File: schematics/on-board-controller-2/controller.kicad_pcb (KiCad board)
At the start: 2 copper layers, 90 x 60 mm, 75 parts, among them J1 5-1814832-1, J2 programmer, J3 xt60, M1 Motor_DC, M2 Motor_DC, M3 Stepper_Motor_bipolar, Q1 NMOS, U1 L293D, U2 STM32L476RGTx, U3 L293D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

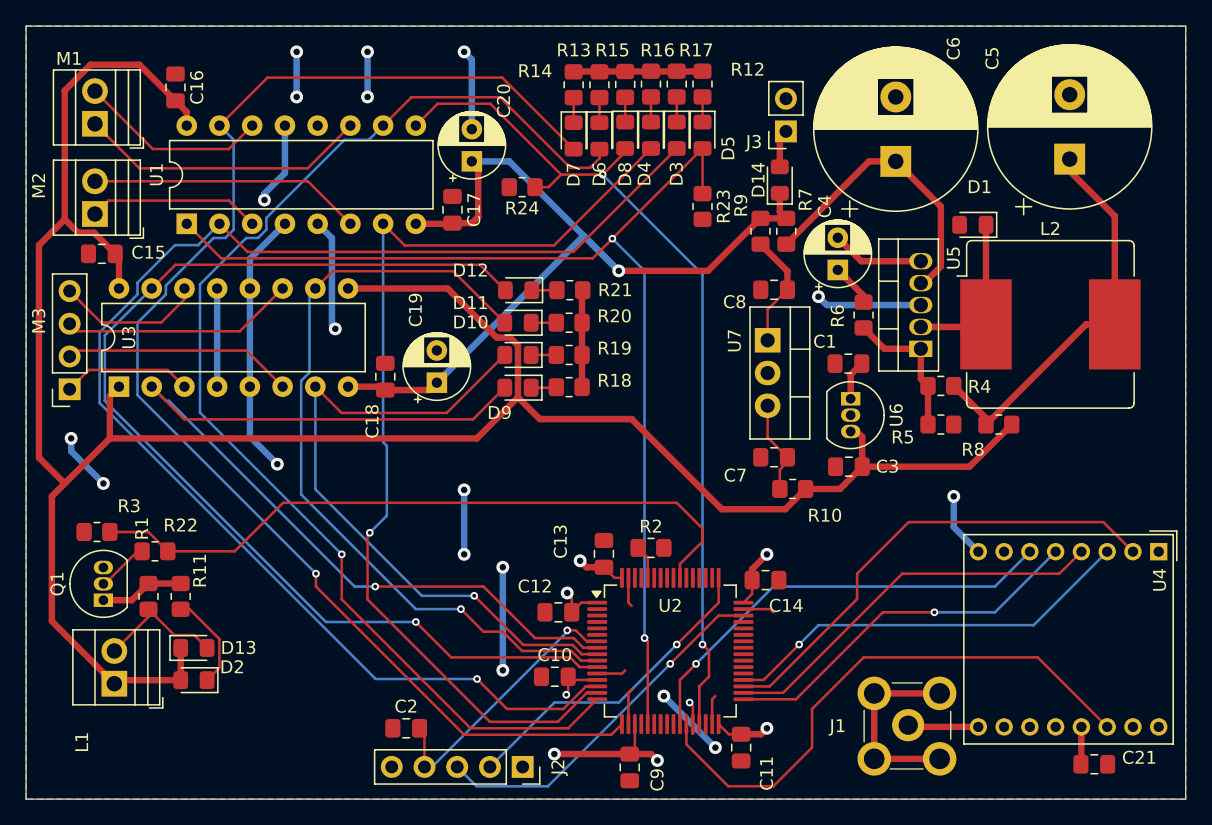
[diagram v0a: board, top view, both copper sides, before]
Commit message: produced version with 2 0V floods
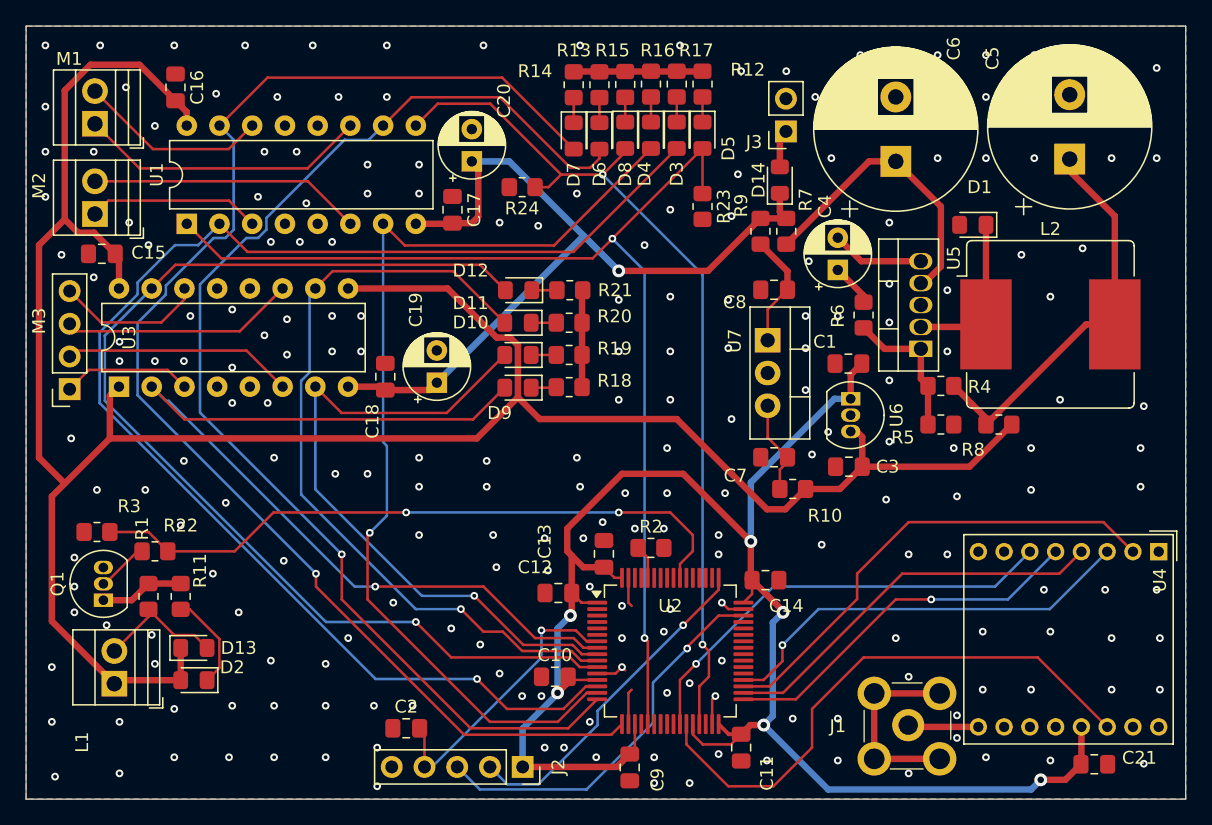
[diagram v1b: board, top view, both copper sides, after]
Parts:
- moved C12 1.50 mm to (103.8, 104.5)
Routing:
- net +3V3: track 40.3 -> 136.9 mm, vias 8 -> 6
- net GND: track 140.5 -> 46.9 mm, vias 18 -> 222
- net /mcu/SWDIO: track 28.3 -> 30.4 mm
- net ELECTROMAGNET: track 53.6 -> 51.6 mm, vias 0 -> 2
- net /mcu/SWCLK: track 25.0 -> 26.1 mm
- net /mcu/RESET: track 21.4 -> 22.5 mm
- net MOSI: track 32.4 -> 33.1 mm
- added copper zone on B.Cu, net GND
- removed copper zone on B.Cu, net +3V3

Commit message: added a keepout zone
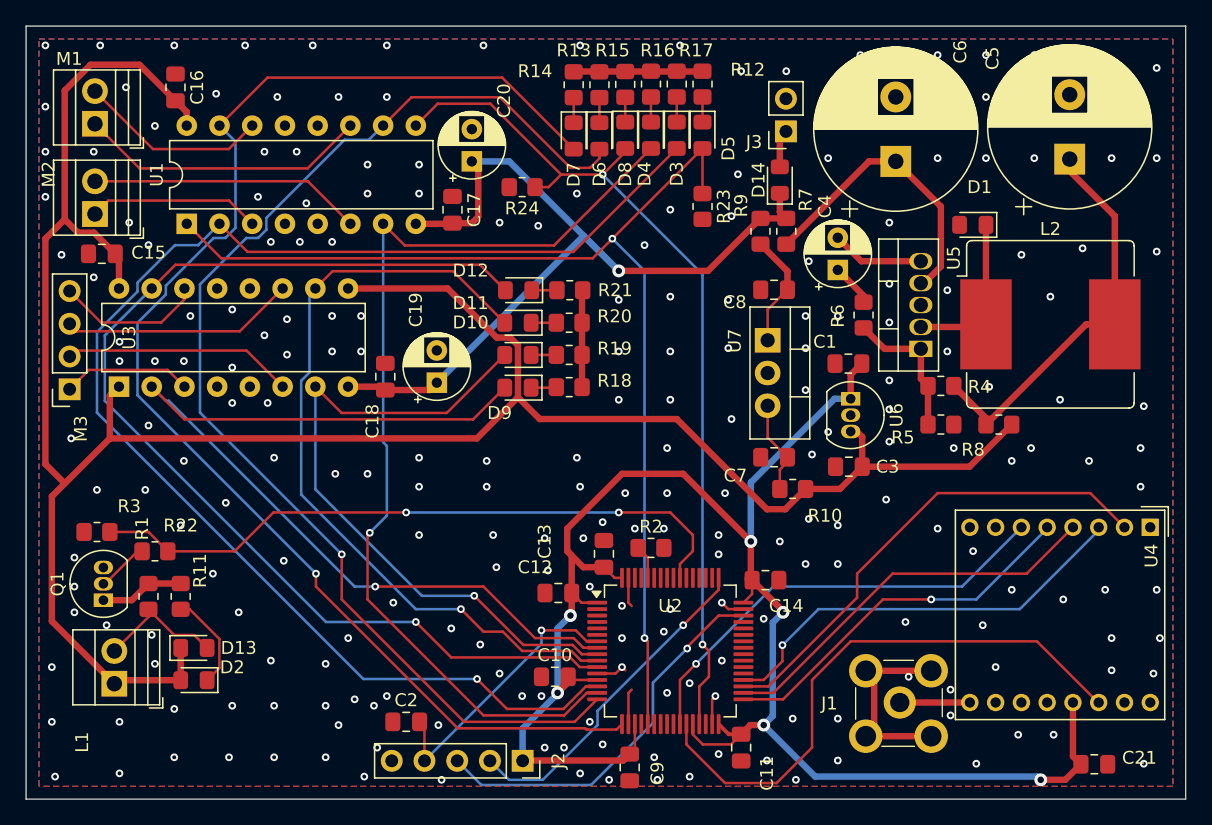
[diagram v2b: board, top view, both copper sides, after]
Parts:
- moved U4 2.00 mm to (149.8, 99.4)
- moved J1 1.88 mm to (130.2, 113.1)
- moved C2 0.50 mm to (92.0, 114.5)
- moved J2 0.47 mm to (101.0, 117.5)
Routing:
- net +3V3: track 136.9 -> 137.7 mm
- net /mcu/RESET: track 22.5 -> 21.7 mm
- net DC_MOTOR1: track 107.7 -> 108.4 mm
- net RADIO_DONE: track 43.7 -> 44.4 mm
- net Net-(U4-ANT): track 5.31 -> 4.78 mm
- net GND: vias 222 -> 237
